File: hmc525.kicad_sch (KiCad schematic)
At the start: 4 parts, among them U1 PAT1220-C-6DB, U2 HMC525ALC4

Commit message: Round 1 review comments
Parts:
- removed U1: PAT1220-C-6DB, RF_Converter:RF_Attenuator_Susumu_PAT1220, symbol RF:PAT1220-C-6DB
- added U?: PAT1220-C-1DB, RF_Converter:RF_Attenuator_Susumu_PAT1220, symbol RF:PAT1220-C-1DB
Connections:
- net GND: now also U?.3
- net HMC788A/RF_{OUT}: now also U?.1
- net at TP1.C: now also U?.2
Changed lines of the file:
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@@
 	)
 	(symbol
-		(lib_id "RF:PAT1220-C-6DB")
+		(lib_id "RF:PAT1220-C-1DB")
 		(at 118.11 167.64 0)
 		(unit 1)
@@
 		(in_pos_files yes)
 		(dnp no)
-		(property "Reference" "U1"
+		(fields_autoplaced yes)
+		(property "Reference" "U?"
 			(at 118.11 157.48 0)
 			(show_name no)
@@
 			)
 		)
-		(property "Value" "PAT1220-C-6DB"
+		(property "Value" "PAT1220-C-1DB"
 			(at 118.11 160.02 0)
 			(show_name no)
@@
 			)
 		)
-		(property "Description" "10GHz RF Attenuator, 50ohm Matched Impedance, 6dB Attenuation, PAT1220"
+		(property "Description" "10GHz RF Attenuator, 50ohm Matched Impedance, 1dB Attenuation, PAT1220"
 			(at 118.11 167.64 0)
 			(hide yes)
@@
 			)
 		)
+		(pin "3"
+		)
+		(pin "1"
+		)
 		(pin "2"
 		)
-		(pin "3"
-		)
-		(pin "1"
-		)
-		(instances
-			(project "huskypointofload"
-				(path "/eb9c972b-d134-41da-be97-ece3f463f7e0/d592dca6-985b-424e-980b-4b036b0ee281"
-					(reference "U1")
-					(unit 1)
-				)
-				(path "/eb9c972b-d134-41da-be97-ece3f463f7e0/ff4f07c4-e191-4e61-a9ef-d50cbe59545f"
-					(reference "U37")
+		(instances
+			(project "huskypointofload"
+				(path "/eb9c972b-d134-41da-be97-ece3f463f7e0/d592dca6-985b-424e-980b-4b036b0ee281"
+					(reference "U?")
+					(unit 1)
+				)
+				(path "/eb9c972b-d134-41da-be97-ece3f463f7e0/ff4f07c4-e191-4e61-a9ef-d50cbe59545f"
+					(reference "U?")
 					(unit 1)
 				)
@@
 				)
 				(path "/eb9c972b-d134-41da-be97-ece3f463f7e0/ff4f07c4-e191-4e61-a9ef-d50cbe59545f"
-					(reference "U38")
+					(reference "U41")
 					(unit 1)
 				)
@@
 		(dnp no)
 		(fields_autoplaced yes)
-		(property "Reference" "#PWR011"
+		(property "Reference" "#PWR014"
 			(at 148.59 189.23 0)
 			(hide yes)
@@
 			(project "huskypointofload"
 				(path "/eb9c972b-d134-41da-be97-ece3f463f7e0/d592dca6-985b-424e-980b-4b036b0ee281"
-					(reference "#PWR011")
-					(unit 1)
-				)
-				(path "/eb9c972b-d134-41da-be97-ece3f463f7e0/ff4f07c4-e191-4e61-a9ef-d50cbe59545f"
-					(reference "#PWR0260")
+					(reference "#PWR014")
+					(unit 1)
+				)
+				(path "/eb9c972b-d134-41da-be97-ece3f463f7e0/ff4f07c4-e191-4e61-a9ef-d50cbe59545f"
+					(reference "#PWR0298")
 					(unit 1)
 				)
@@
 		(dnp no)
 		(fields_autoplaced yes)
-		(property "Reference" "#PWR010"
+		(property "Reference" "#PWR013"
 			(at 118.11 189.23 0)
 			(hide yes)
@@
 			(project "huskypointofload"
 				(path "/eb9c972b-d134-41da-be97-ece3f463f7e0/d592dca6-985b-424e-980b-4b036b0ee281"
-					(reference "#PWR010")
-					(unit 1)
-				)
-				(path "/eb9c972b-d134-41da-be97-ece3f463f7e0/ff4f07c4-e191-4e61-a9ef-d50cbe59545f"
-					(reference "#PWR0259")
+					(reference "#PWR013")
+					(unit 1)
+				)
+				(path "/eb9c972b-d134-41da-be97-ece3f463f7e0/ff4f07c4-e191-4e61-a9ef-d50cbe59545f"
+					(reference "#PWR0297")
 					(unit 1)
 				)
@@
 				)
 				(path "/eb9c972b-d134-41da-be97-ece3f463f7e0/ff4f07c4-e191-4e61-a9ef-d50cbe59545f"
-					(reference "TP21")
+					(reference "TP22")
 					(unit 1)
 				)
@@
 		(dnp no)
 		(fields_autoplaced yes)
-		(property "Reference" "#PWR012"
+		(property "Reference" "#PWR015"
 			(at 189.23 189.23 0)
 			(hide yes)
@@
 			(project "huskypointofload"
 				(path "/eb9c972b-d134-41da-be97-ece3f463f7e0/d592dca6-985b-424e-980b-4b036b0ee281"
-					(reference "#PWR012")
-					(unit 1)
-				)
-				(path "/eb9c972b-d134-41da-be97-ece3f463f7e0/ff4f07c4-e191-4e61-a9ef-d50cbe59545f"
-					(reference "#PWR0261")
+					(reference "#PWR015")
+					(unit 1)
+				)
+				(path "/eb9c972b-d134-41da-be97-ece3f463f7e0/ff4f07c4-e191-4e61-a9ef-d50cbe59545f"
+					(reference "#PWR0299")
 					(unit 1)
 				)
@@
 				)
 				(path "/eb9c972b-d134-41da-be97-ece3f463f7e0/ff4f07c4-e191-4e61-a9ef-d50cbe59545f"
-					(reference "TP22")
-					(unit 1)
-				)
+					(reference "TP23")
+					(unit 1)
+				)

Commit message: Round 2 Review, power tree cleanup
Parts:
- added FL1: LFCN-8440, Filter:Filter_Mini-Circuits_FV1206-4, symbol RF_Filter:LFCN-8440
- gave numbers to parts that had none: 1
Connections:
- net GND: now also FL1.2 (GND), FL1.4 (GND)
- net HMC788A/RF_{OUT}: now also FL1.1 (IN); no longer U1.1
- new net: FL1.3 (OUT), U1.1
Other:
- sheet HMC788A ports: added 5VIN; removed 6VIN
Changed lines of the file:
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@@
+	(wire
+		(pts
+			(xy 102.87 165.1) (xy 107.95 165.1)
+		)
+		(stroke
+			(width 0)
+			(type default)
+		)
+	)
 	(wire
 		(pts
@@
 	(wire
 		(pts
+			(xy 92.71 175.26) (xy 92.71 182.88)
+		)
+		(stroke
+			(width 0)
+			(type default)
+		)
+	)
+	(wire
+		(pts
 			(xy 189.23 180.34) (xy 189.23 177.8)
 		)
@@
 	(wire
 		(pts
-			(xy 69.85 165.1) (xy 77.47 165.1)
+			(xy 41.91 165.1) (xy 49.53 165.1)
 		)
 		(stroke
@@
 	(wire
 		(pts
-			(xy 69.85 161.29) (xy 77.47 161.29)
+			(xy 41.91 161.29) (xy 49.53 161.29)
 		)
 		(stroke
@@
 	(wire
 		(pts
-			(xy 102.87 165.1) (xy 107.95 165.1)
+			(xy 74.93 165.1) (xy 82.55 165.1)
 		)
 		(stroke
@@
 		)
 	)
-	(hierarchical_label "6V"
+	(hierarchical_label "5V"
 		(shape input)
-		(at 69.85 161.29 180)
+		(at 41.91 161.29 180)
 		(effects
 			(font
@@
 	(hierarchical_label "LO"
 		(shape input)
-		(at 69.85 165.1 180)
+		(at 41.91 165.1 180)
 		(effects
 			(font
@@
 			)
 			(justify right)
+		)
+	)
+	(symbol
+		(lib_id "power:GND")
+		(at 92.71 182.88 0)
+		(unit 1)
+		(body_style 1)
+		(exclude_from_sim no)
+		(in_bom yes)
+		(on_board yes)
+		(in_pos_files yes)
+		(dnp no)
+		(fields_autoplaced yes)
+		(property "Reference" "#PWR015"
+			(at 92.71 189.23 0)
+			(hide yes)
+			(show_name no)
+			(do_not_autoplace no)
+			(effects
+				(font
+					(size 1.27 1.27)
+				)
+			)
+		)
+		(property "Value" "GND"
+			(at 92.71 187.96 0)
+			(show_name no)
+			(do_not_autoplace no)
+			(effects
+				(font
+					(size 1.27 1.27)
+				)
+			)
+		)
+		(property "Footprint" ""
+			(at 92.71 182.88 0)
+			(hide yes)
+			(show_name no)
+			(do_not_autoplace no)
+			(effects
+				(font
+					(size 1.27 1.27)
+				)
+			)
+		)
+		(property "Datasheet" ""
+			(at 92.71 182.88 0)
+			(hide yes)
+			(show_name no)
+			(do_not_autoplace no)
+			(effects
+				(font
+					(size 1.27 1.27)
+				)
+			)
+		)
+		(property "Description" "Power symbol creates a global label with name \"GND\" , ground"
+			(at 92.71 182.88 0)
+			(hide yes)
+			(show_name no)
+			(do_not_autoplace no)
+			(effects
+				(font
+					(size 1.27 1.27)
+				)
+			)
+		)
+		(pin "1"
+		)
+		(instances
+			(project "huskypointofload"
+				(path "/eb9c972b-d134-41da-be97-ece3f463f7e0/d592dca6-985b-424e-980b-4b036b0ee281"
+					(reference "#PWR015")
+					(unit 1)
+				)
+				(path "/eb9c972b-d134-41da-be97-ece3f463f7e0/ff4f07c4-e191-4e61-a9ef-d50cbe59545f"
+					(reference "#PWR0307")
+					(unit 1)
+				)
+			)
 		)
 	)
@@
 		(dnp no)
 		(fields_autoplaced yes)
-		(property "Reference" "U?"
+		(property "Reference" "U1"
 			(at 118.11 157.48 0)
 			(show_name no)
@@
 			(project "huskypointofload"
 				(path "/eb9c972b-d134-41da-be97-ece3f463f7e0/d592dca6-985b-424e-980b-4b036b0ee281"
-					(reference "U?")
+					(reference "U1")
 					(unit 1)
 				)
 				(path "/eb9c972b-d134-41da-be97-ece3f463f7e0/ff4f07c4-e191-4e61-a9ef-d50cbe59545f"
-					(reference "U?")
+					(reference "U41")
 					(unit 1)
 				)
@@
 				)
 				(path "/eb9c972b-d134-41da-be97-ece3f463f7e0/ff4f07c4-e191-4e61-a9ef-d50cbe59545f"
-					(reference "U41")
+					(reference "U42")
 					(unit 1)
 				)
@@
 		(dnp no)
 		(fields_autoplaced yes)
-		(property "Reference" "#PWR014"
+		(property "Reference" "#PWR017"
 			(at 148.59 189.23 0)
 			(hide yes)
@@
 			(project "huskypointofload"
 				(path "/eb9c972b-d134-41da-be97-ece3f463f7e0/d592dca6-985b-424e-980b-4b036b0ee281"
-					(reference "#PWR014")
+					(reference "#PWR017")
 					(unit 1)
 				)
 				(path "/eb9c972b-d134-41da-be97-ece3f463f7e0/ff4f07c4-e191-4e61-a9ef-d50cbe59545f"
-					(reference "#PWR0298")
+					(reference "#PWR0309")
 					(unit 1)
 				)
@@
 		(dnp no)
 		(fields_autoplaced yes)
-		(property "Reference" "#PWR013"
+		(property "Reference" "#PWR016"
 			(at 118.11 189.23 0)
 			(hide yes)
@@
 			(project "huskypointofload"
 				(path "/eb9c972b-d134-41da-be97-ece3f463f7e0/d592dca6-985b-424e-980b-4b036b0ee281"
-					(reference "#PWR013")
+					(reference "#PWR016")
 					(unit 1)
 				)
 				(path "/eb9c972b-d134-41da-be97-ece3f463f7e0/ff4f07c4-e191-4e61-a9ef-d50cbe59545f"
-					(reference "#PWR0297")
+					(reference "#PWR0308")
 					(unit 1)
 				)
@@
 		(dnp no)
 		(fields_autoplaced yes)
-		(property "Reference" "#PWR015"
+		(property "Reference" "#PWR018"
 			(at 189.23 189.23 0)
 			(hide yes)
@@
 			(project "huskypointofload"
 				(path "/eb9c972b-d134-41da-be97-ece3f463f7e0/d592dca6-985b-424e-980b-4b036b0ee281"
-					(reference "#PWR015")
+					(reference "#PWR018")
 					(unit 1)
 				)
 				(path "/eb9c972b-d134-41da-be97-ece3f463f7e0/ff4f07c4-e191-4e61-a9ef-d50cbe59545f"
-					(reference "#PWR0299")
+					(reference "#PWR0310")
 					(unit 1)
 				)
@@
 		)
 	)
+	(symbol
+		(lib_id "RF_Filter:LFCN-8440")
+		(at 92.71 165.1 0)
+		(unit 1)
+		(body_style 1)
+		(exclude_from_sim no)
+		(in_bom yes)
+		(on_board yes)
+		(in_pos_files yes)
+		(dnp no)
+		(fields_autoplaced yes)
+		(property "Reference" "FL1"
+			(at 92.71 152.4 0)
+			(show_name no)
+			(do_not_autoplace no)
+			(effects
+				(font
+					(size 1.27 1.27)
+				)
+			)
+		)
+		(property "Value" "LFCN-8440"
+			(at 92.71 154.94 0)
+			(show_name no)
+			(do_not_autoplace no)
+			(effects
+				(font
+					(size 1.27 1.27)
+				)
+			)
+		)
+		(property "Footprint" "Filter:Filter_Mini-Circuits_FV1206-4"
+			(at 92.71 152.4 0)
+			(hide yes)
+			(show_name no)
+			(do_not_autoplace no)
+			(effects
+				(font
+					(size 1.27 1.27)
+				)
+			)
+		)
+		(property "Datasheet" "https://www.minicircuits.com/pdfs/LFCN-8440+.pdf"
+			(at 92.71 165.1 0)
+			(hide yes)
+			(show_name no)
+			(do_not_autoplace no)
+			(effects
+				(font
+					(size 1.27 1.27)
+				)
+			)
+		)
+		(property "Description" "8440MHz 50 Ohm Passive Low Pass Filter, FV1206-4"
+			(at 92.71 165.1 0)
+			(hide yes)
+			(show_name no)
+			(do_not_autoplace no)
+			(effects
+				(font
+					(size 1.27 1.27)
+				)
+			)
+		)
+		(pin "1"
+		)
+		(pin "2"
+		)
+		(pin "4"
+		)
+		(pin "3"
+		)
+		(instances
+			(project "huskypointofload"
+				(path "/eb9c972b-d134-41da-be97-ece3f463f7e0/d592dca6-985b-424e-980b-4b036b0ee281"
+					(reference "FL1")
+					(unit 1)
+				)
+				(path "/eb9c972b-d134-41da-be97-ece3f463f7e0/ff4f07c4-e191-4e61-a9ef-d50cbe59545f"
+					(reference "FL2")
+					(unit 1)
+				)
+			)
+		)
+	)
 	(sheet
-		(at 77.47 158.75)
+		(at 49.53 158.75)
 		(size 25.4 12.7)
 		(exclude_from_sim no)
@@
 		)
 		(property "Sheetname" "HMC788A"
-			(at 77.47 158.0384 0)
+			(at 49.53 158.0384 0)
 			(show_name no)
 			(do_not_autoplace no)
@@
 		)
 		(property "Sheetfile" "hmc788.kicad_sch"
-			(at 77.47 172.0346 0)
+			(at 49.53 172.0346 0)
 			(show_name no)
 			(do_not_autoplace no)
@@
 			)
 		)
-		(pin "6VIN" input
-			(at 77.47 161.29 180)
+		(pin "RF_{IN}" input
+			(at 49.53 165.1 180)
 			(effects
 				(font
@@
 			)
 		)
-		(pin "RF_{IN}" input
-			(at 77.47 165.1 180)
+		(pin "RF_{OUT}" input
+			(at 74.93 165.1 0)
+			(effects
+				(font
+					(size 1.27 1.27)
+				)
+				(justify right)
+			)
+		)
+		(pin "5VIN" input
+			(at 49.53 161.29 180)
 			(effects
 				(font
@@
 			)
 		)
-		(pin "RF_{OUT}" input
-			(at 102.87 165.1 0)
-			(effects
-				(font
-					(size 1.27 1.27)
-				)
-				(justify right)
-			)
-		)

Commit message: Darrel Suggestions
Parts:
- added FL2, FL3: LFCN-2000, Filter:Filter_Mini-Circuits_FV1206, symbol RF_Filter:LFCN-2000
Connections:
- net GND: now also FL2.2 (GND), FL2.4 (GND), FL3.2 (GND), FL3.4 (GND)
- net I: now also FL2.3 (OUT); no longer U2.9 (IF1)
- net Q: now also FL3.3 (OUT); no longer U2.11 (IF2)
- new net: FL3.1 (IN), U2.11 (IF2)
- new net: FL2.1 (IN), U2.9 (IF1)

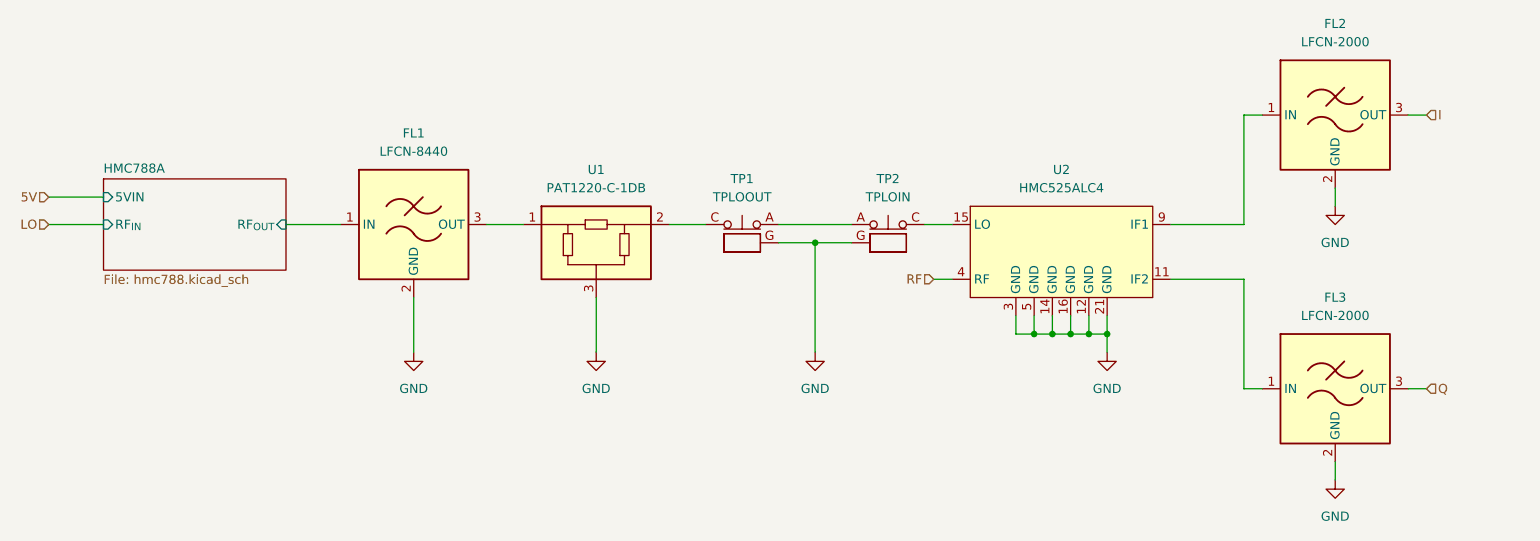
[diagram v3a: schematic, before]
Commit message: add NC and fix ERC
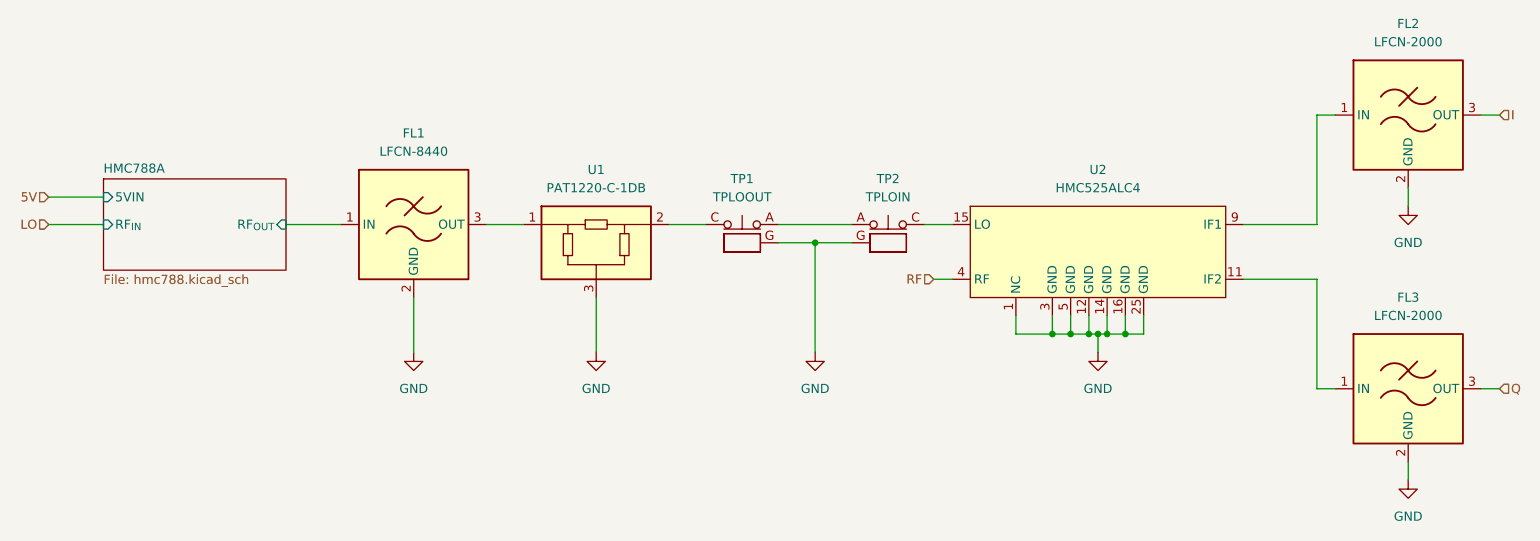
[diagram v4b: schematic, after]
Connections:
- net GND: now also U2.1 (NC), U2.10 (NC), U2.13 (NC), U2.17 (NC), U2.18 (NC), U2.19 (NC), U2.2 (NC), U2.20 (NC), U2.22 (NC), U2.23 (NC), U2.24 (NC), U2.25 (GND), U2.6 (NC), U2.7 (NC), U2.8 (NC)
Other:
- moved on the sheet: FL2, FL3
